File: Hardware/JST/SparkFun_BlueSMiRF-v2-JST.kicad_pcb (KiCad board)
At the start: 2 copper layers, 40.1 x 15.2 mm, 51 parts, among them J1 JST_Locking_6, Q1 BSS138, Q2 BSS138, SW1 SMD_4.6x2.8mm_h2.5mm, U1 ESP32-PICO-V3-02, U2 AP2112K-3.3

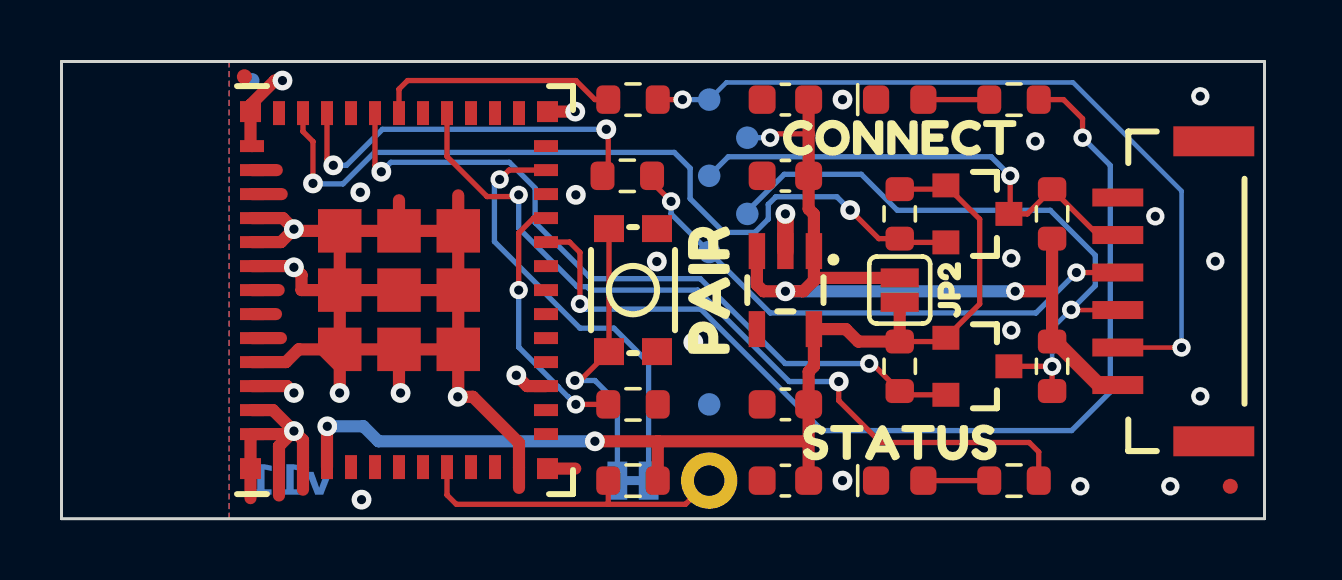
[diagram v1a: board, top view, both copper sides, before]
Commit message: Design Update
Update symbols and footprints based on latest SparkFun library
Extended board length to line up with grid layout: 1.5" -> 1.6"
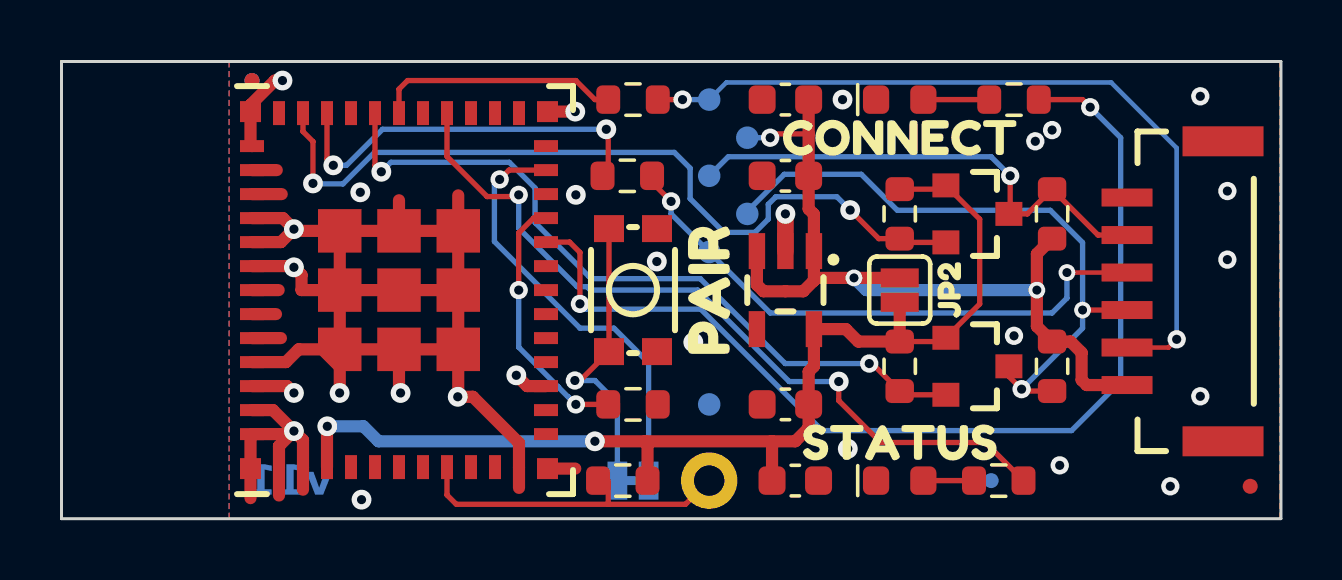
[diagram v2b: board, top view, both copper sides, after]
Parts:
- J1: footprint SparkFun-Connector:JST_SMD_1.25mm-6_Locking -> SparkFun-Connector:JST_1x06_P1.25mm_Locking_Horizontal_SMD
- TP1: footprint SparkFun-Connector:1x01 -> SparkFun-Connector:1x01_P2.54mm
- moved kibuzzard-655A532D 0.66 mm to (166.6, 130.7)
- moved FID2 0.66 mm to (169.2, 131.0)
- moved kibuzzard-65022EAF 0.66 mm to (167.7, 118.4)
- moved kibuzzard-655A4397 0.66 mm to (167.6, 123.6)
- moved kibuzzard-655A43AA 0.66 mm to (167.5, 120.9)
- moved kibuzzard-655A4470 0.66 mm to (167.8, 128.4)
- moved kibuzzard-655A4492 0.66 mm to (167.5, 126.1)
- moved R6 0.51 mm to (160.8, 130.8), turned to 0 degrees
- moved R1 0.34 mm to (148.2, 130.8), turned to 0 degrees
- moved C4 0.33 mm to (154.0, 130.8), turned to 0 degrees
- moved J1 0.31 mm to (166.8, 124.5)
- moved FID1 0.28 mm to (135.9, 117.5)
- turned R10 to 90 degrees
- turned R3 to 180 degrees
- turned R4 to 180 degrees
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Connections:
- R1 pad 1: 3.3V -> Net-(U1-EN)
- R1 pad 2: Net-(U1-EN) -> 3.3V
- R10 pad 1: ~{RTS_HV} -> VCC
- R10 pad 2: VCC -> ~{RTS_HV}
- R2 pad 1: GND -> Net-(U1-IOA15)
- R2 pad 2: Net-(U1-IOA15) -> GND
- R3 pad 1: RX_LV -> RX_HV
- R3 pad 2: RX_HV -> RX_LV
- R4 pad 1: ~{CTS_LV} -> ~{CTS_HV}
- R4 pad 2: ~{CTS_HV} -> ~{CTS_LV}
- R5 pad 1: /Connect -> Net-(D1-A)
- R5 pad 2: Net-(D1-A) -> /Connect
- R6 pad 1: /Status -> Net-(D2-A)
- R6 pad 2: Net-(D2-A) -> /Status
- R7 pad 1: TX_LV -> 3.3V
- R7 pad 2: 3.3V -> TX_LV
- R8 pad 1: ~{RTS_LV} -> 3.3V
- R8 pad 2: 3.3V -> ~{RTS_LV}
- R9 pad 1: TX_HV -> VCC
- R9 pad 2: VCC -> TX_HV
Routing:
- net VCC: track 29.5 -> 28.1 mm
- net /Status: track 27.3 -> 26.2 mm
- net ~{CTS_HV}: track 18.3 -> 19.2 mm
- net /Connect: track 34.2 -> 34.8 mm
- net Net-(D2-A): track 2.20 -> 1.69 mm
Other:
- board size 40.1 x 15.2 mm -> 40.6 x 15.2 mm
- board text removed: "N. Seidle"

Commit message: Update PCB
- Move fiducial location
- Add ground via
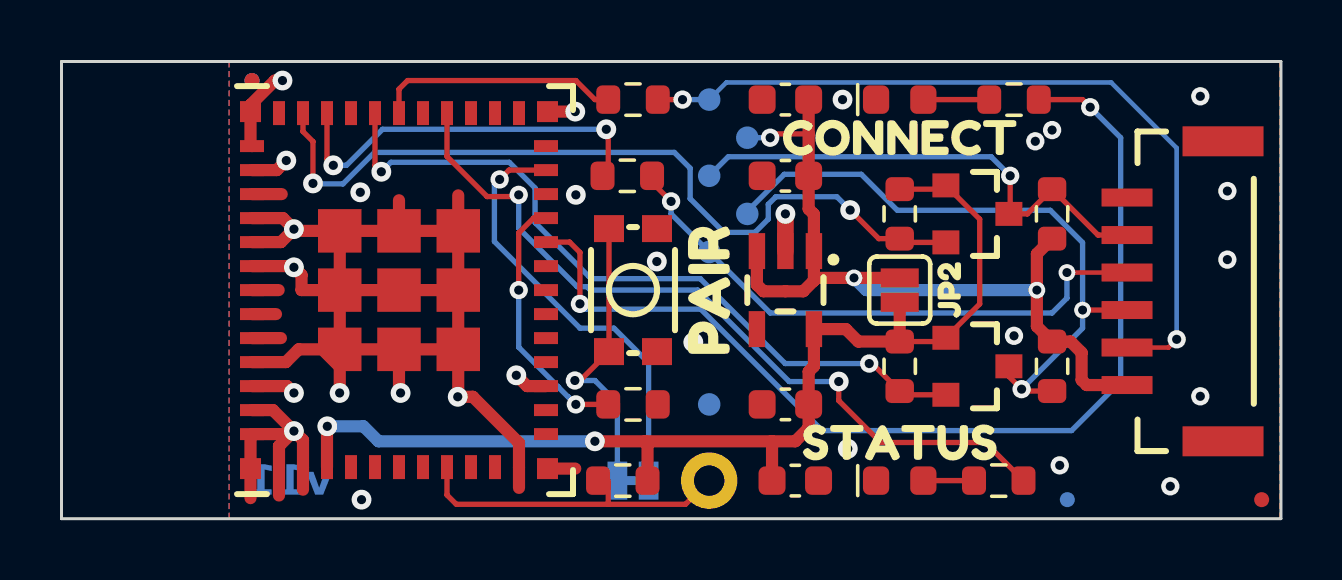
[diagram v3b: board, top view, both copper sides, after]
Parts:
- moved FID4 2.62 mm to (163.1, 131.4)
- moved FID2 0.59 mm to (169.5, 131.4)
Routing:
- net GND: track 64.7 -> 65.1 mm, vias 27 -> 28
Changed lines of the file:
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@@
 	(footprint "SparkFun-Aesthetic:Fiducial_0.5mm_Mask1mm"
 		(layer "F.Cu")
-		(at 169.164 131)
+		(at 169.545 131.445)
 		(descr "Circular Fiducial, 0.5mm bare copper, 1mm soldermask opening (Level C)")
 		(tags "SparkFun fiducial")
@@
 	(footprint "SparkFun-Aesthetic:Fiducial_0.5mm_Mask1mm"
 		(layer "B.Cu")
-		(at 160.528 130.81 180)
+		(at 163.068 131.445 180)
 		(descr "Circular Fiducial, 0.5mm bare copper, 1mm soldermask opening (Level C)")
 		(tags "SparkFun fiducial")
@@
 	)
 	(segment
-		(start 135.89 120.46)
-		(end 136.716 120.46)
-		(width 0.4064)
-		(layer "F.Cu")
-		(net 1)
-	)
-	(segment
 		(start 135.89 129.26)
 		(end 137.186 129.26)
@@
 	)
 	(segment
+		(start 136.715 120.46)
+		(end 137.033 120.142)
+		(width 0.4064)
+		(layer "F.Cu")
+		(net 1)
+	)
+	(segment
 		(start 137.247 123.66)
 		(end 137.287 123.7)
@@
 	)
 	(segment
+		(start 135.89 120.46)
+		(end 136.715 120.46)
+		(width 0.4064)
+		(layer "F.Cu")
+		(net 1)
+	)
+	(segment
 		(start 135.84 118.287)
 		(end 135.84 118.51)
@@
 		(net 1)
 	)
+	(via
+		(at 137.033 120.142)
+		(size 0.6604)
+		(drill 0.3048)
+		(layers "F.Cu" "B.Cu")
+		(net 1)
+	)

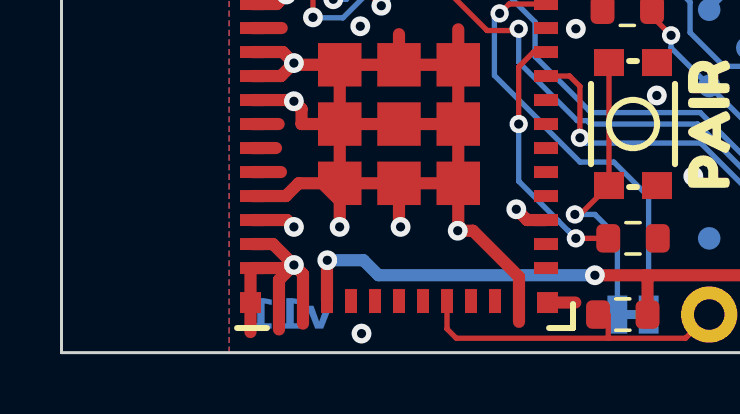
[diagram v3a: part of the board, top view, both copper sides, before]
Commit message: Change version text
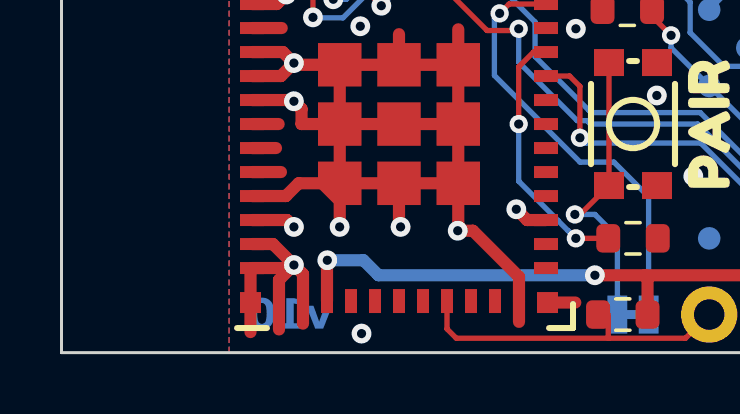
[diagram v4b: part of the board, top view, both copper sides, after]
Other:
- board text added: "v10"
- board text removed: "v11"
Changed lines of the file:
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@@
 		(layer "User.1")
 	)
-	(gr_text "v11"
+	(gr_text "v10"
 		(at 137.16 130.81 0)
 		(layer "B.Cu" knockout)
@@
 			(keep_text_aligned yes)
 		)
-		(gr_text "0.60 in"
+		(gr_text "15.2 mm"
 			(at 125.85 124.46 90)
 			(layer "User.1")
@@
 			(keep_text_aligned yes)
 		)
-		(gr_text "1.60 in"
+		(gr_text "40.64 mm"
 			(at 149.86 133.47 0)
 			(layer "User.1")
